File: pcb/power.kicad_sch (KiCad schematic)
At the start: 23 parts, among them J13 SM04B-SRSS-TB, J2 USB_C_USB2.0_16P, U2 LM66200DRLR, U3 USBLC6-2P6, U6 LM66200DRLR, U7 AZ1084-3.3

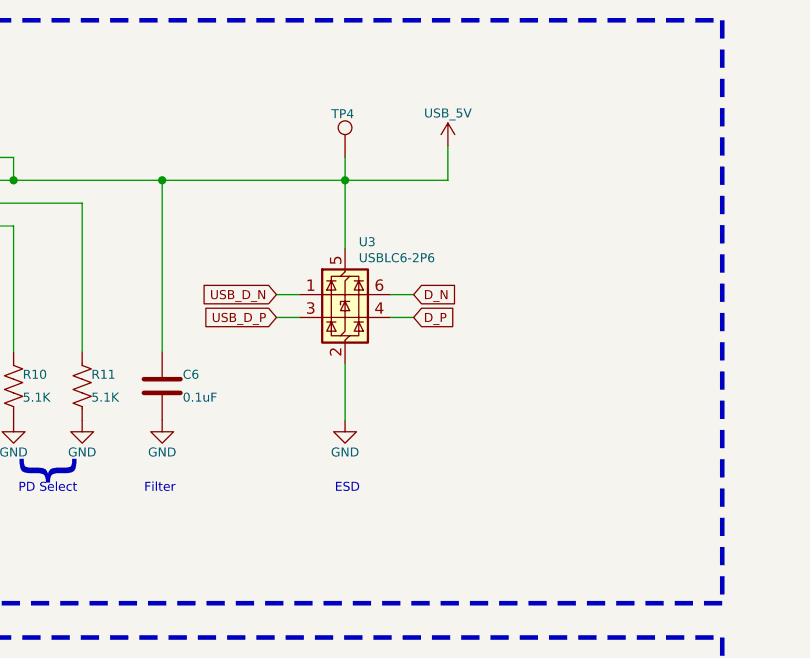
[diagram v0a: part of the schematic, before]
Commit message: Added test points. Fixed license file.
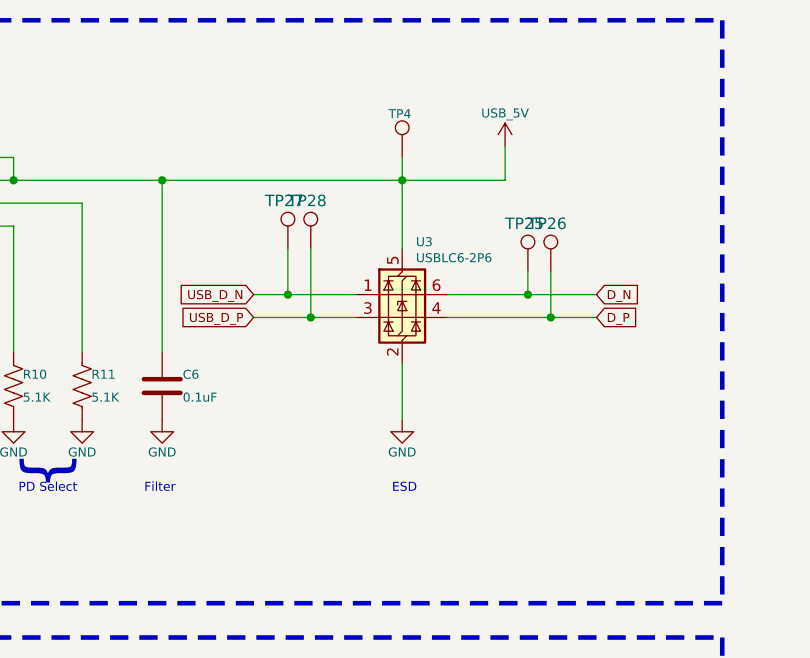
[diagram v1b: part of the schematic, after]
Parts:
- added TP25, TP26, TP27, TP28: TP, CRGM Mechanical:TestPoint_Pad_D1.0mm, symbol Connector:TestPoint
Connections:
- net D_N: now also TP25.1
- net D_P: now also TP26.1
- net USB_D_N: now also TP27.1
- net USB_D_P: now also TP28.1
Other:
- moved on the sheet: TP4, U3

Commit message: Change name in schematic
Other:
- title: Node Hardware -> Hub Hardware
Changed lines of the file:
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@@
 	(paper "A4")
 	(title_block
-		(title "Node Hardware")
+		(title "Hub Hardware")
 		(date "<<release-date>>")
 		(rev "<<tag>>")

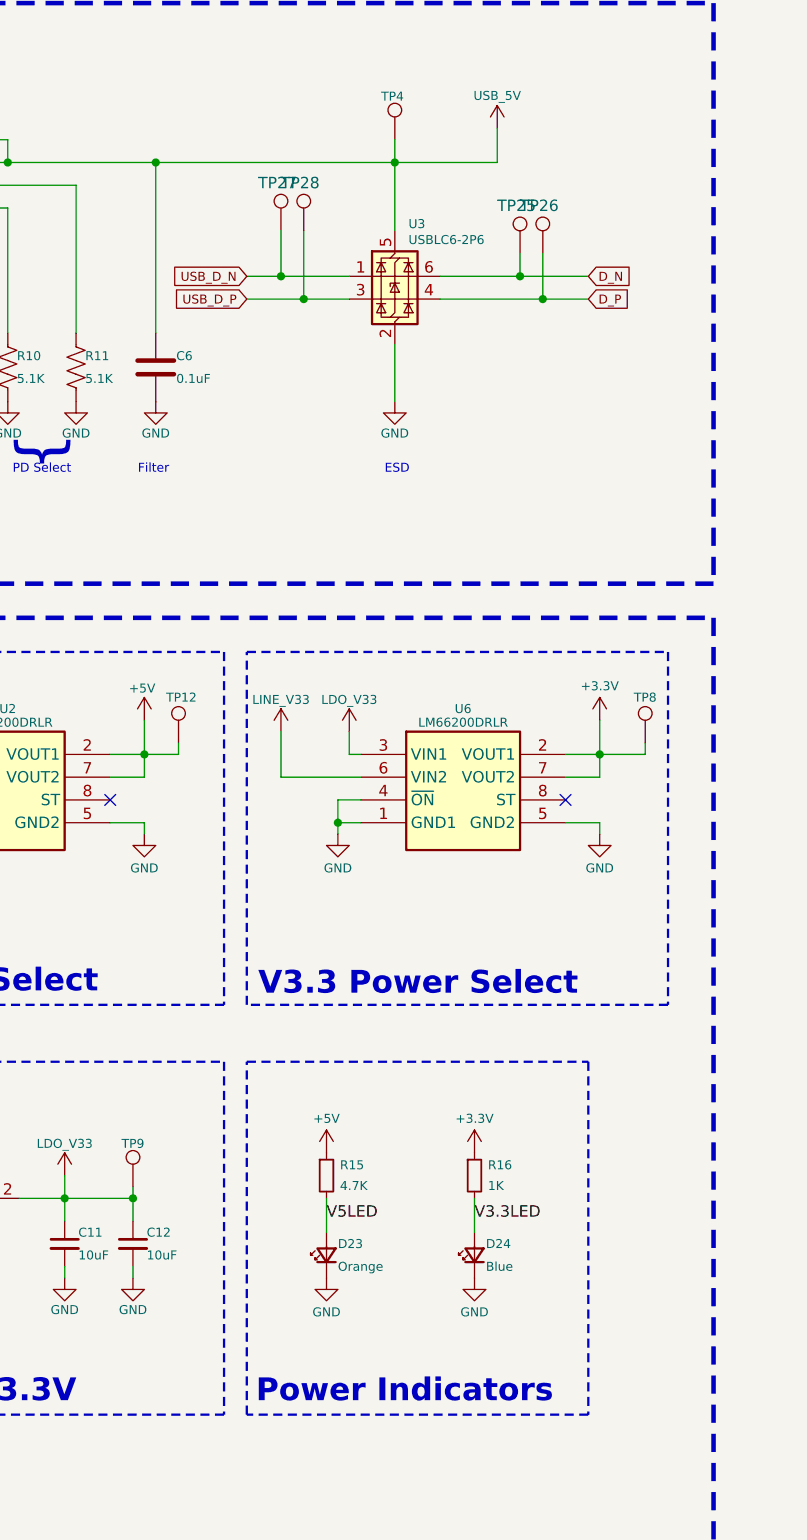
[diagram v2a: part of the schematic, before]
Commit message: Renamed files; update with more test points
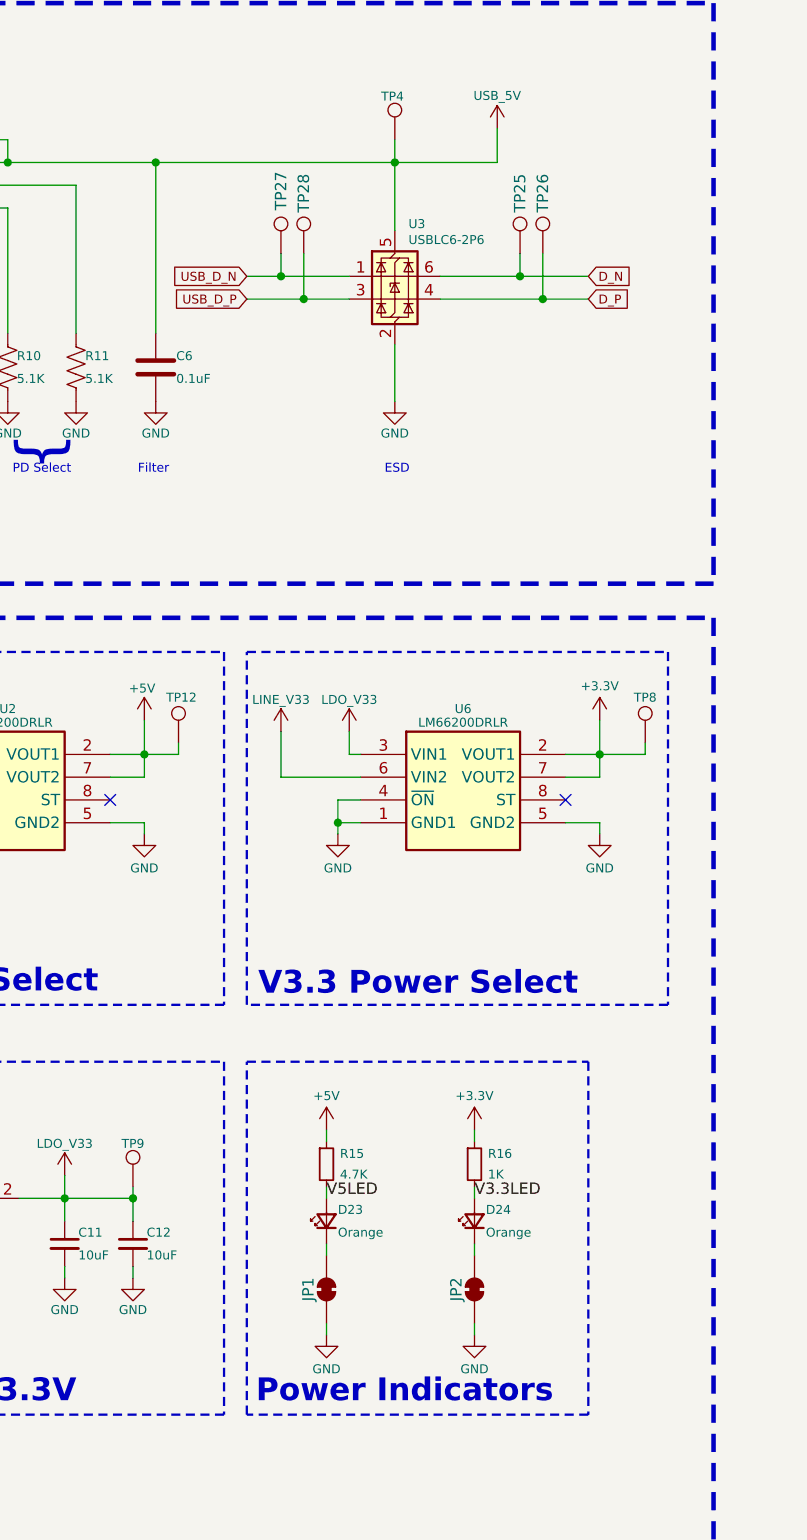
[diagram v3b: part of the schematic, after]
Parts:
- added JP1, JP2: ~, symbol Jumper:SolderJumper_2_Bridged
- D24: value Blue -> Orange; Digikey 5962-XL-1608UBC-04TR-ND -> 5962-XL-1608UOC-06TR-ND; LCSC C965807 -> C965800; MPN XL-1608UBC-04 -> XL-1608UOC-06; Mouser 710-150060BS75020 -> 859-LTST-C190KFKT
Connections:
- net GND: now also JP1.1 (A), JP2.1 (A); no longer D23.1 (K), D24.1 (K)
- new net: D23.1 (K), JP1.2 (B)
- new net: D24.1 (K), JP2.2 (B)
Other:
- moved on the sheet: D23, R15, R16, TP27, TP28

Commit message: Renamed peripherals to interfaces; added test points; added led jumper
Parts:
- JP1, JP2: footprint (none) -> CRGM Connector:SolderJumper-2_P1.3mm_Bridged_RoundedPad1.0x1.5mm
- TP10, TP11, TP12, TP25, TP26, TP27, TP28, TP4, TP8, TP9: value TP -> ~
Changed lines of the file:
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@@
 			)
 		)
-		(property "Value" "TP"
+		(property "Value" "~"
 			(at 118.11 36.068 0)
 			(effects
@@
 			)
 		)
-		(property "Value" "TP"
+		(property "Value" "~"
 			(at 115.57 36.068 0)
 			(effects
@@
 			)
 		)
-		(property "Value" "TP"
+		(property "Value" "~"
 			(at 21.59 99.314 0)
 			(effects
@@
 			)
 		)
-		(property "Footprint" ""
+		(property "Footprint" "CRGM Connector:SolderJumper-2_P1.3mm_Bridged_RoundedPad1.0x1.5mm"
 			(at 118.11 158.75 0)
 			(effects
@@
 			)
 		)
-		(property "Value" "TP"
+		(property "Value" "~"
 			(at 152.146 92.456 0)
 			(effects
@@
 			)
 		)
-		(property "Value" "TP"
+		(property "Value" "~"
 			(at 142.24 36.068 0)
 			(effects
@@
 			)
 		)
-		(property "Value" "TP"
+		(property "Value" "~"
 			(at 26.162 91.694 0)
 			(effects
@@
 			)
 		)
-		(property "Value" "TP"
+		(property "Value" "~"
 			(at 126.746 28.448 0)
 			(effects
@@
 			)
 		)
-		(property "Value" "TP"
+		(property "Value" "~"
 			(at 144.78 36.068 0)
 			(effects
@@
 			)
 		)
-		(property "Value" "TP"
+		(property "Value" "~"
 			(at 93.472 141.986 0)
 			(effects
@@
 			)
 		)
-		(property "Value" "TP"
+		(property "Value" "~"
 			(at 102.616 92.71 0)
 			(effects
@@
 			)
 		)
-		(property "Footprint" ""
+		(property "Footprint" "CRGM Connector:SolderJumper-2_P1.3mm_Bridged_RoundedPad1.0x1.5mm"
 			(at 134.62 158.75 0)
 			(effects

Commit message: Adjusting for consistency
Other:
- title: Hub Hardware -> Aquarius Hub
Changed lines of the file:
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@@
 	(paper "A4")
 	(title_block
-		(title "Hub Hardware")
+		(title "Aquarius Hub")
 		(date "<<release-date>>")
 		(rev "<<tag>>")

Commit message: Sync symbols and footprints
Transitioned to CRGM footprints
Added dimensions
Fixed some spacing
Adjusted properties
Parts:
- C11, C12, C6: footprint Capacitor_SMD:C_0603_1608Metric -> CRGM Passive:C_0603_1608Metric
- J13: Mouser 306-BM04BSRSSTBTLFSN -> 306-SM04BSRSSTBTLFSN
- R10, R11, R15, R16: footprint Resistor_SMD:R_0603_1608Metric -> CRGM Passive:R_0603_1608Metric
- U3: footprint Package_TO_SOT_SMD:SOT-666 -> CRGM Passive:SOT-666
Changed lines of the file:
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@@
 			)
 		)
-		(property "Footprint" "Resistor_SMD:R_0603_1608Metric"
+		(property "Footprint" "CRGM Passive:R_0603_1608Metric"
 			(at 118.11 144.78 0)
 			(effects
@@
 			)
 		)
-		(property "Footprint" "Capacitor_SMD:C_0603_1608Metric"
+		(property "Footprint" "CRGM Passive:C_0603_1608Metric"
 			(at 89.8652 157.48 0)
 			(effects
@@
 		)
 		(property "Footprint" "CRGM Connector:GCT_USB4105-GF-A"
-			(at 53.34 45.72 0)
+			(at 49.53 93.218 0)
 			(effects
 				(font
@@
 		)
 		(property "MN" "GTC"
-			(at 49.53 45.72 0)
+			(at 49.53 84.582 0)
 			(effects
 				(font
@@
 		)
 		(property "MPN" "USB4105-GF-A-060"
-			(at 49.53 45.72 0)
+			(at 49.53 86.36 0)
 			(effects
 				(font
@@
 		)
 		(property "Mouser" "640-USB4105-GF-A-060"
-			(at 49.53 45.72 0)
+			(at 49.53 88.646 0)
 			(effects
 				(font
@@
 		)
 		(property "Digikey" "2073-USB4105-GF-A-060TR-ND"
-			(at 49.53 45.72 0)
+			(at 49.53 91.186 0)
 			(effects
 				(font
@@
 		)
 		(property "LCSC" "C165948"
-			(at 49.53 45.72 0)
+			(at 49.53 95.25 0)
 			(effects
 				(font
@@
 			)
 		)
-		(property "Footprint" "Capacitor_SMD:C_0603_1608Metric"
+		(property "Footprint" "CRGM Passive:C_0603_1608Metric"
 			(at 100.0252 59.69 0)
 			(effects
@@
 			)
 		)
-		(property "Footprint" "Resistor_SMD:R_0603_1608Metric"
+		(property "Footprint" "CRGM Passive:R_0603_1608Metric"
 			(at 91.186 56.134 90)
 			(effects
@@
 			)
 		)
-		(property "Description" "JST SH 1.0mm 4 Position Horizontal"
+		(property "Description" "4 Position, 1mm pitch"
 			(at 46.228 113.792 0)
 			(effects
@@
 			)
 		)
-		(property "Mouser" "306-BM04BSRSSTBTLFSN"
+		(property "Mouser" "306-SM04BSRSSTBTLFSN"
 			(at 46.736 118.872 0)
 			(effects
@@
 			)
 		)
-		(property "Footprint" "Package_TO_SOT_SMD:SOT-666"
+		(property "Footprint" "CRGM Passive:SOT-666"
 			(at 126.746 52.451 0)
 			(effects
@@
 			)
 		)
-		(property "Footprint" "Capacitor_SMD:C_0603_1608Metric"
+		(property "Footprint" "CRGM Passive:C_0603_1608Metric"
 			(at 97.4852 157.48 0)
 			(effects
@@
 			)
 		)
-		(property "Footprint" "Resistor_SMD:R_0603_1608Metric"
+		(property "Footprint" "CRGM Passive:R_0603_1608Metric"
 			(at 134.62 144.78 0)
 			(effects
@@
 			)
 		)
-		(property "Footprint" "Resistor_SMD:R_0603_1608Metric"
+		(property "Footprint" "CRGM Passive:R_0603_1608Metric"
 			(at 83.566 56.134 90)
 			(effects

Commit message: Clean up and consistency
Moved buzzer to MCU
Fixed model directory
Set font size
Set outline size
Upscaled Roxy ❤️
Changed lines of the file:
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@@
 	(rectangle
 		(start 15.24 83.82)
-		(end 161.29 190.5)
+		(end 161.29 177.8)
 		(stroke
 			(width 0.508)
@@
 	(text "USB"
 		(exclude_from_sim yes)
-		(at 24.638 75.438 0)
+		(at 15.24 80.01 0)
 		(effects
 			(font
 				(face "KiCad Font")
-				(size 5.08 5.08)
+				(size 3 3)
 				(thickness 1.016)
 				(bold yes)
-				(color 255 153 0 1)
-			)
+				(color 0 0 194 1)
+			)
+			(justify left bottom)
 		)
 	)
@@
 	(text "Power"
 		(exclude_from_sim yes)
-		(at 28.194 186.436 0)
+		(at 15.24 177.8 0)
 		(effects
 			(font
 				(face "KiCad Font")
-				(size 5.08 5.08)
+				(size 3 3)
 				(thickness 1.016)
 				(bold yes)
-				(color 255 153 0 1)
-			)
-		)
-	)
+				(color 0 0 194 1)
+			)
+			(justify left bottom)
+		)
+	)

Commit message: Updated part attributes for consistency.
Updated requirements section to be more accurate.
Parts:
- C11, C12, C6: Tolerance (none) -> 10%
- R10, R11, R15, R16: Tolerance (none) -> 5%
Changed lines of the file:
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@@
 			)
 		)
+		(property "Tolerance" "5%"
+			(at 118.11 144.78 0)
+			(effects
+				(font
+					(size 1.27 1.27)
+				)
+				(hide yes)
+			)
+		)
 		(pin "1"
 		)
@@
 			)
 		)
+		(property "Tolerance" "10%"
+			(at 88.9 153.67 0)
+			(effects
+				(font
+					(size 1.27 1.27)
+				)
+				(hide yes)
+			)
+		)
 		(pin "2"
 		)
@@
 			)
 		)
+		(property "Tolerance" "10%"
+			(at 99.06 55.88 0)
+			(effects
+				(font
+					(size 1.27 1.27)
+				)
+				(hide yes)
+			)
+		)
 		(pin "1"
 		)
@@
 			)
 		)
+		(property "Tolerance" "5%"
+			(at 90.17 55.88 0)
+			(effects
+				(font
+					(size 1.27 1.27)
+				)
+				(hide yes)
+			)
+		)
 		(pin "2"
 		)
@@
 			)
 		)
+		(property "Tolerance" "10%"
+			(at 96.52 153.67 0)
+			(effects
+				(font
+					(size 1.27 1.27)
+				)
+				(hide yes)
+			)
+		)
 		(pin "2"
 		)
@@
 			)
 		)
+		(property "Tolerance" "5%"
+			(at 134.62 144.78 0)
+			(effects
+				(font
+					(size 1.27 1.27)
+				)
+				(hide yes)
+			)
+		)
 		(pin "1"
 		)
@@
 			(at 82.55 55.88 0)
 			(effects
+				(font
+					(size 1.27 1.27)
+				)
+				(hide yes)
+			)
+		)
+		(property "Tolerance" "5%"
+			(at 82.55 55.88 0)
+			(effects
